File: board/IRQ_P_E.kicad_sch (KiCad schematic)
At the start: 19 parts, among them U14 74F32, U15 74F00, U23 74F11, U37 74LS148, U38 74LS08, U39 74LS148, U40 74F157, U51 74F157, U60 CY7C192, U61 CY7C192

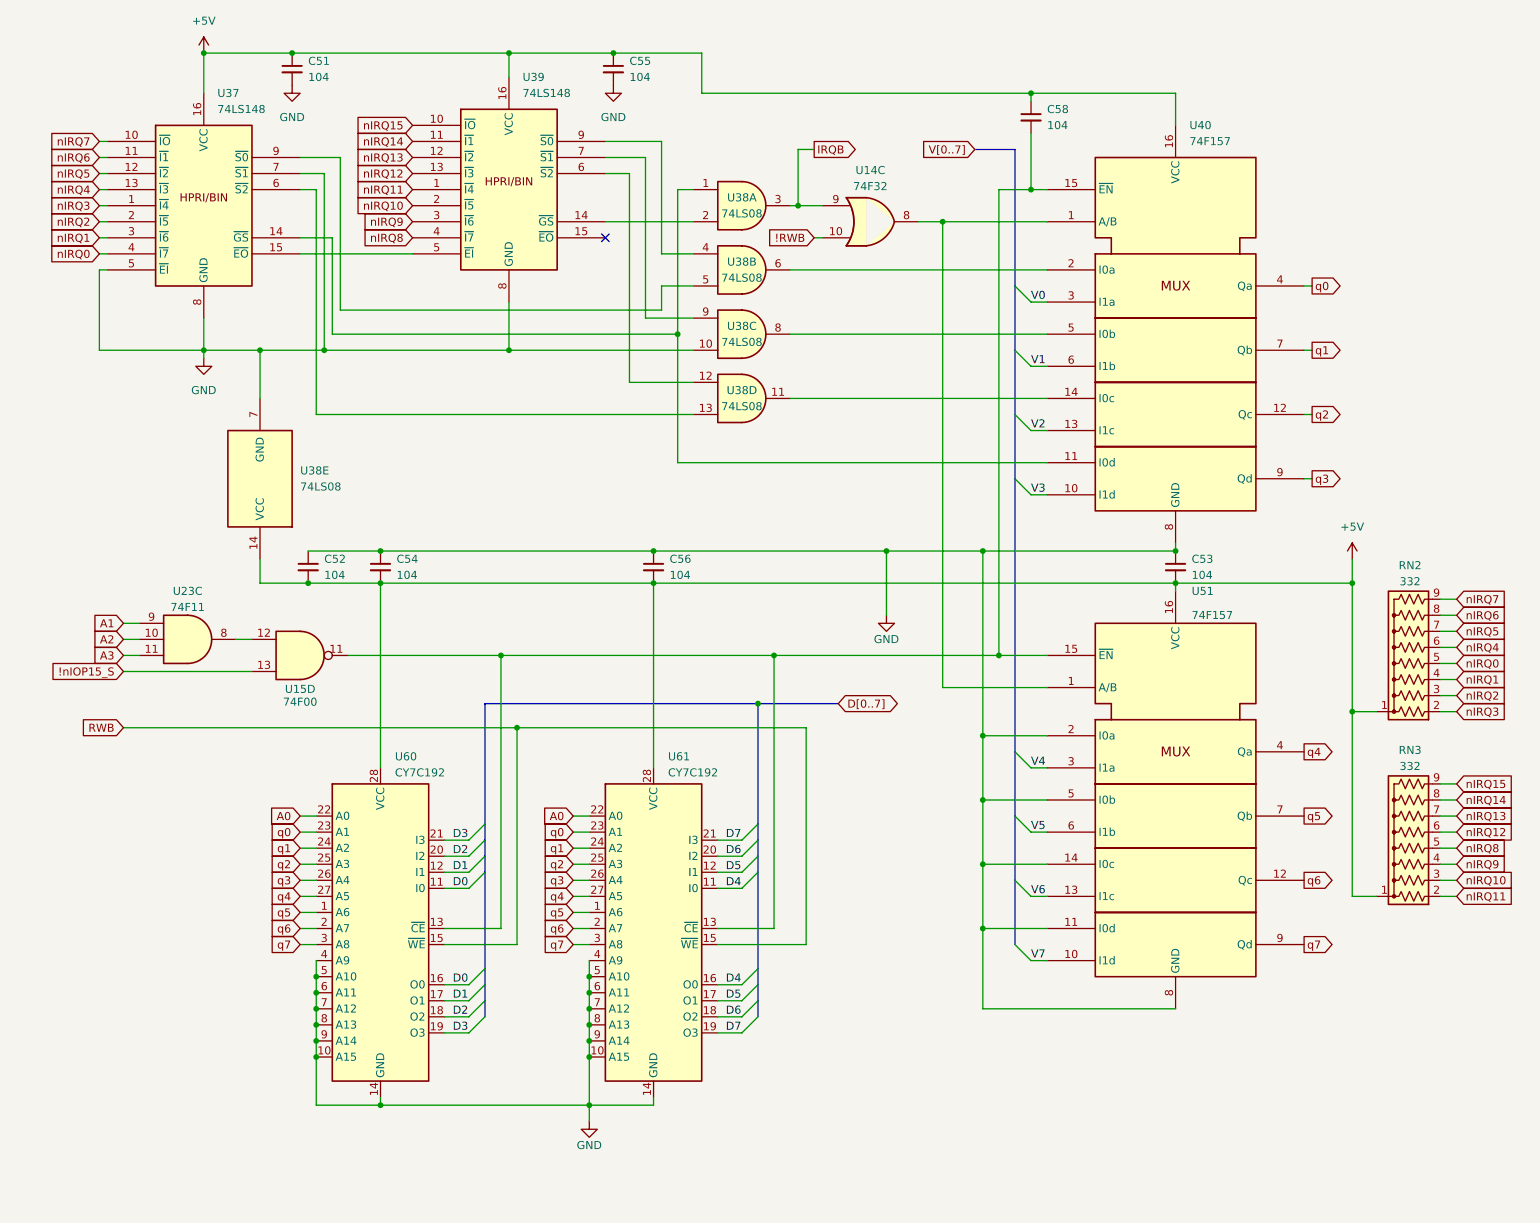
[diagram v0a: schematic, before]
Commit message: V2.0: wait states, GAL glue logic, serial clock and review fixes
Main board schematic:
- Replace the T4-T7 clock divider with RDY wait states. Fixed 7.16 MHz
  CPU clock; J36 selects 3.58 MHz for Rockwell parts. Waits are set per
  region through the write-only register at $FFF5 (reset = 3 waits).
- Move address decode, strobes, the wait-state generator, the IRQ
  encoder/latch/vector mux, ROM bank gating and DMA sync into seven GALs
  (U81-U86 ATF22V10C, U87 ATF16V8C), removing 29 ICs. CUPL sources,
  JEDECs and notes are in board/PLDs/V2.
- 1.8432 MHz serial clock, soft-power latch, -5V regulator, bulk caps,
  pull-ups, audio coupling/decoupling, GNDA tie, read-only Z register
  and other design-review fixes.
- New WaitStates and Support sheets; project symbol library
  hydra16.kicad_sym with sym-lib-table.

PCB updated from the schematic. Includes pending changes to the counter,
bus breakout and memory daughter card projects.

Firmware:
- Remove S_REGISTER; T/U/V/W now at $FFF0-$FFF3 to match the hardware.
- Add math.s and sound.s (included by os_main.s).
- Rebuild the 65C02 ROM image.

Co-Authored-By: Claude Opus 5.5 <noreply@anthropic.com>
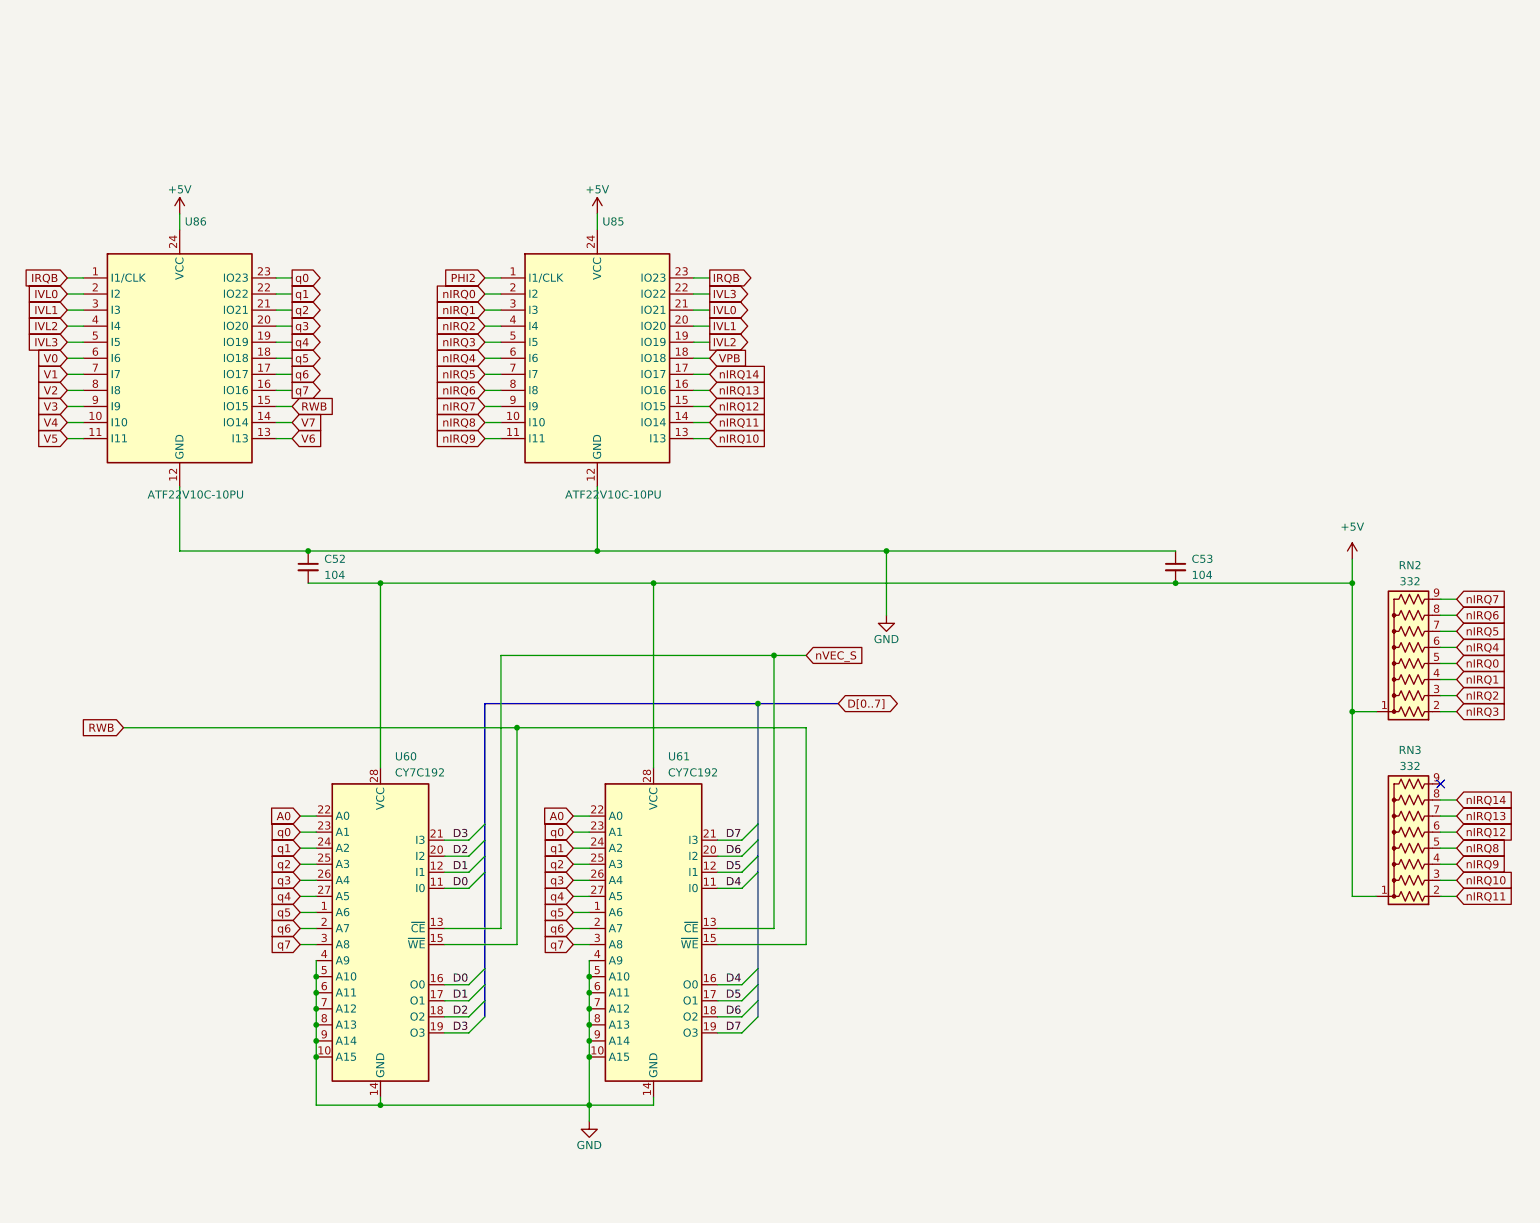
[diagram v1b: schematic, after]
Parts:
- removed C51, C54, C55, C56, C58: 104, Capacitor_THT:C_Disc_D5.0mm_W2.5mm_P5.00mm, symbol Device:C_Small
- removed U14: 74F32, Package_DIP:DIP-14_W7.62mm_Socket_LongPads, symbol 74xx:74LS32
- removed U15: 74F00, Package_DIP:DIP-14_W7.62mm_Socket_LongPads, symbol 74xx:74LS00
- removed U23: 74F11, Package_DIP:DIP-14_W7.62mm_Socket_LongPads, symbol 74xx:74LS11
- removed U37, U39: 74LS148, Package_DIP:DIP-16_W7.62mm_Socket_LongPads, symbol 74xx_IEEE:74148
- removed U38: 74LS08, Package_DIP:DIP-14_W7.62mm_Socket_LongPads, symbol 74xx:74LS08
- removed U40, U51: 74F157, Package_DIP:DIP-16_W7.62mm_Socket_LongPads, symbol 74xx_IEEE:74157
- added U85, U86: ATF22V10C-10PU, Package_DIP:DIP-24_W7.62mm_Socket_LongPads, symbol Hydra16:ATF22V10C
- U60, U61: footprint Package_DIP:DIP-28_W15.24mm_Socket_LongPads -> Package_DIP:DIP-28_W7.62mm_Socket_LongPads; symbol 65XX:6551 -> Hydra16:CY7C192
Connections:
- net +5V: now also U85.24 (VCC), U86.24 (VCC)
- net GND: now also U85.12 (GND), U86.12 (GND)
- net IRQB: now also U85.23 (IO23), U86.1 (I1/CLK)
- net RWB: now also U86.15 (IO15)
- net V0: now also U86.6 (I6)
- net V1: now also U86.7 (I7)
- net V2: now also U86.8 (I8)
- net V3: now also U86.9 (I9)
- net V4: now also U86.10 (I10)
- net V5: now also U86.11 (I11)
- net V6: now also U86.13 (I13)
- net V7: now also U86.14 (IO14)
- net nIRQ0: now also U85.2 (I2)
- net nIRQ1: now also U85.3 (I3)
- net nIRQ10: now also U85.13 (I13)
- net nIRQ11: now also U85.14 (IO14)
- net nIRQ12: now also U85.15 (IO15)
- net nIRQ13: now also U85.16 (IO16)
- net nIRQ14: now also U85.17 (IO17)
- net nIRQ2: now also U85.4 (I4)
- net nIRQ3: now also U85.5 (I5)
- net nIRQ4: now also U85.6 (I6)
- net nIRQ5: now also U85.7 (I7)
- net nIRQ6: now also U85.8 (I8)
- net nIRQ7: now also U85.9 (I9)
- net nIRQ8: now also U85.10 (I10)
- net nIRQ9: now also U85.11 (I11)
- net q0: now also U86.23 (IO23)
- net q1: now also U86.22 (IO22)
- net q2: now also U86.21 (IO21)
- net q3: now also U86.20 (IO20)
- net q4: now also U86.19 (IO19)
- net q5: now also U86.18 (IO18)
- net q6: now also U86.17 (IO17)
- net q7: now also U86.16 (IO16)
- net nVEC_S: now reaches U60.13 (~{CE}), U61.13 (~{CE})
- net nIRQ15: no longer names the net of RN3.9 (R8)
- new net IVL0: U85.21 (IO21), U86.2 (I2)
- new net IVL1: U85.20 (IO20), U86.3 (I3)
- new net IVL2: U85.19 (IO19), U86.4 (I4)
- new net IVL3: U85.22 (IO22), U86.5 (I5)
- new net PHI2: U85.1 (I1/CLK)
- new net VPB: U85.18 (IO18)

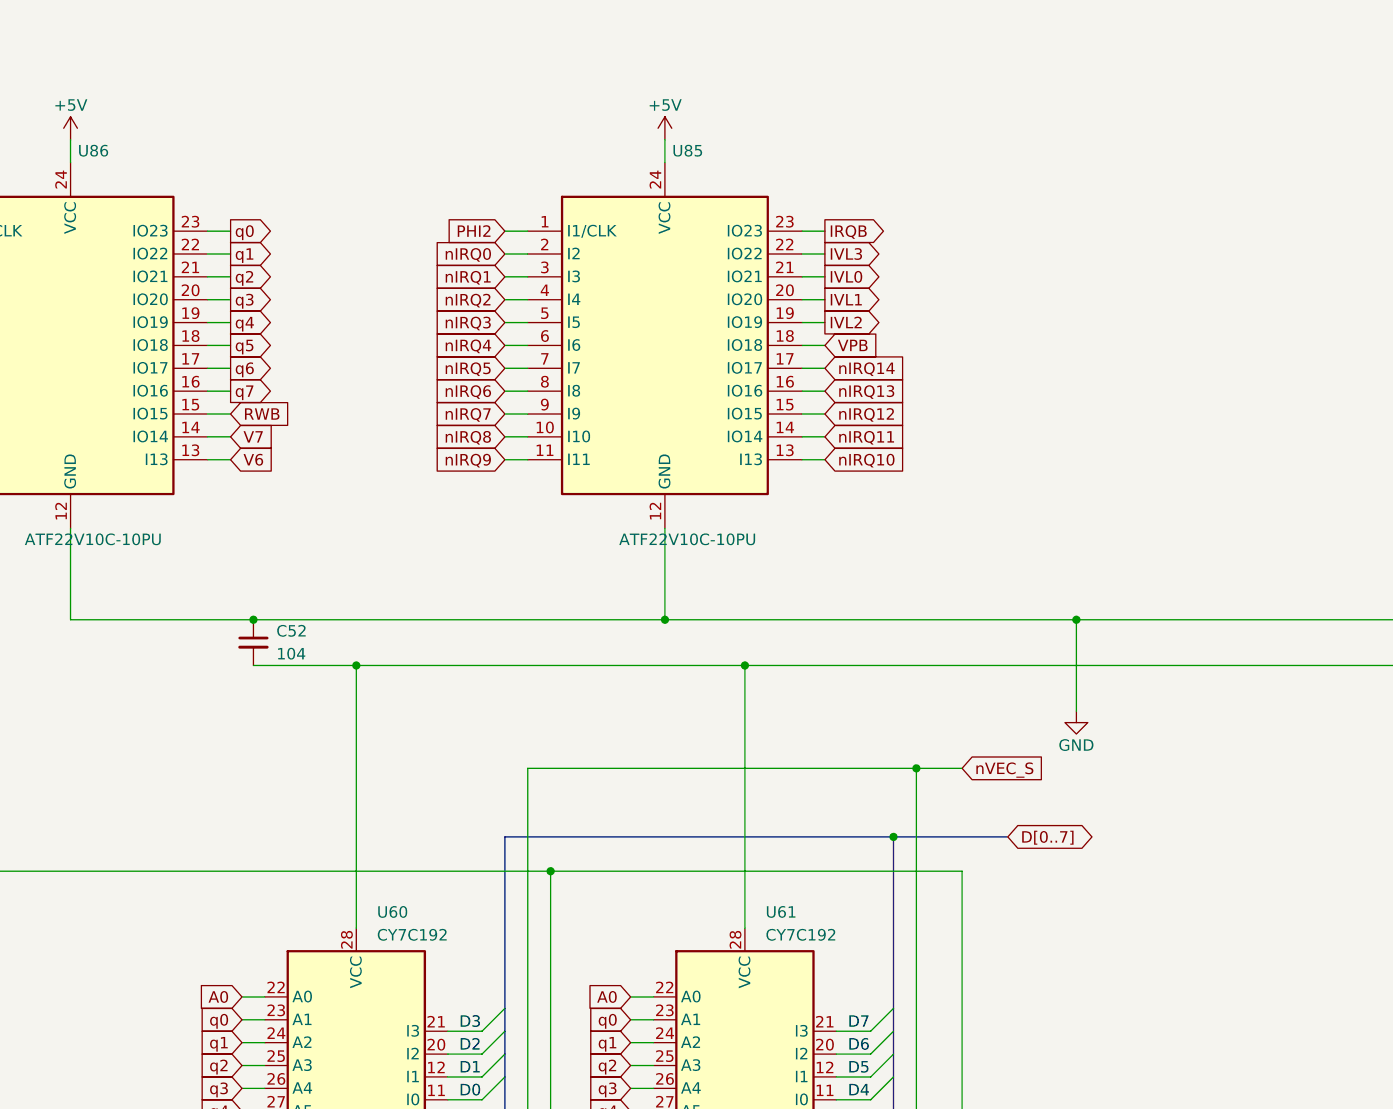
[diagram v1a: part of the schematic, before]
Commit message: V2.0 rev 2.0D: clock stretching, OS ROM paging and review fixes
Bus timing:
- New GAL C (U88) generates PHI2/PHI1 and the 3.58 MHz sound clock from
  the 14.318 MHz master, replacing the U35 74F191 divider. J36 now selects
  7.16 or 3.58 MHz.
- Banked RAM, banked ROM and slot I/O ($FF20-$FFEF) get one extra PHI2-low
  period plus 0-3 extra PHI2-high periods set in $FFF5 (GAL D). This
  replaces the on-board RDY wait generator; cards can still pull RDY.
- Write strobes are now hold-time safe: PHI1 comes straight from GAL C
  and RWB_M straight from GAL B2.

Review fixes:
- OS ROM chip enable from a single-level decode, output enable from
  GAL B1; -55 part specified. Full 4K OS ROM paging via GAL G.
- Vector RAM writes only during PHI2; $FFF0-$FFFF no longer slowed.
- YM2151 /WR on RWB_M. U62 removed. RB0-RB7 pull-ups (RN5).
- Slot clocks driven through U56 and U34 with 33R series resistors.
- J38 enables in-system flashing of the banked ROMs.
- W65C22S/W65C51N, AS6C4008, DS1813-5 and CY7C192-25 values; R4 1k.
- J7 pin 8 no longer +5V; +5VA renamed +5VSB; serial handshake loop.
- Sheet titles and revisions, slot symbol pin fixes, and project symbol
  and footprint libraries so the project opens on another machine.

Co-Authored-By: Claude Opus 5.5 <noreply@anthropic.com>
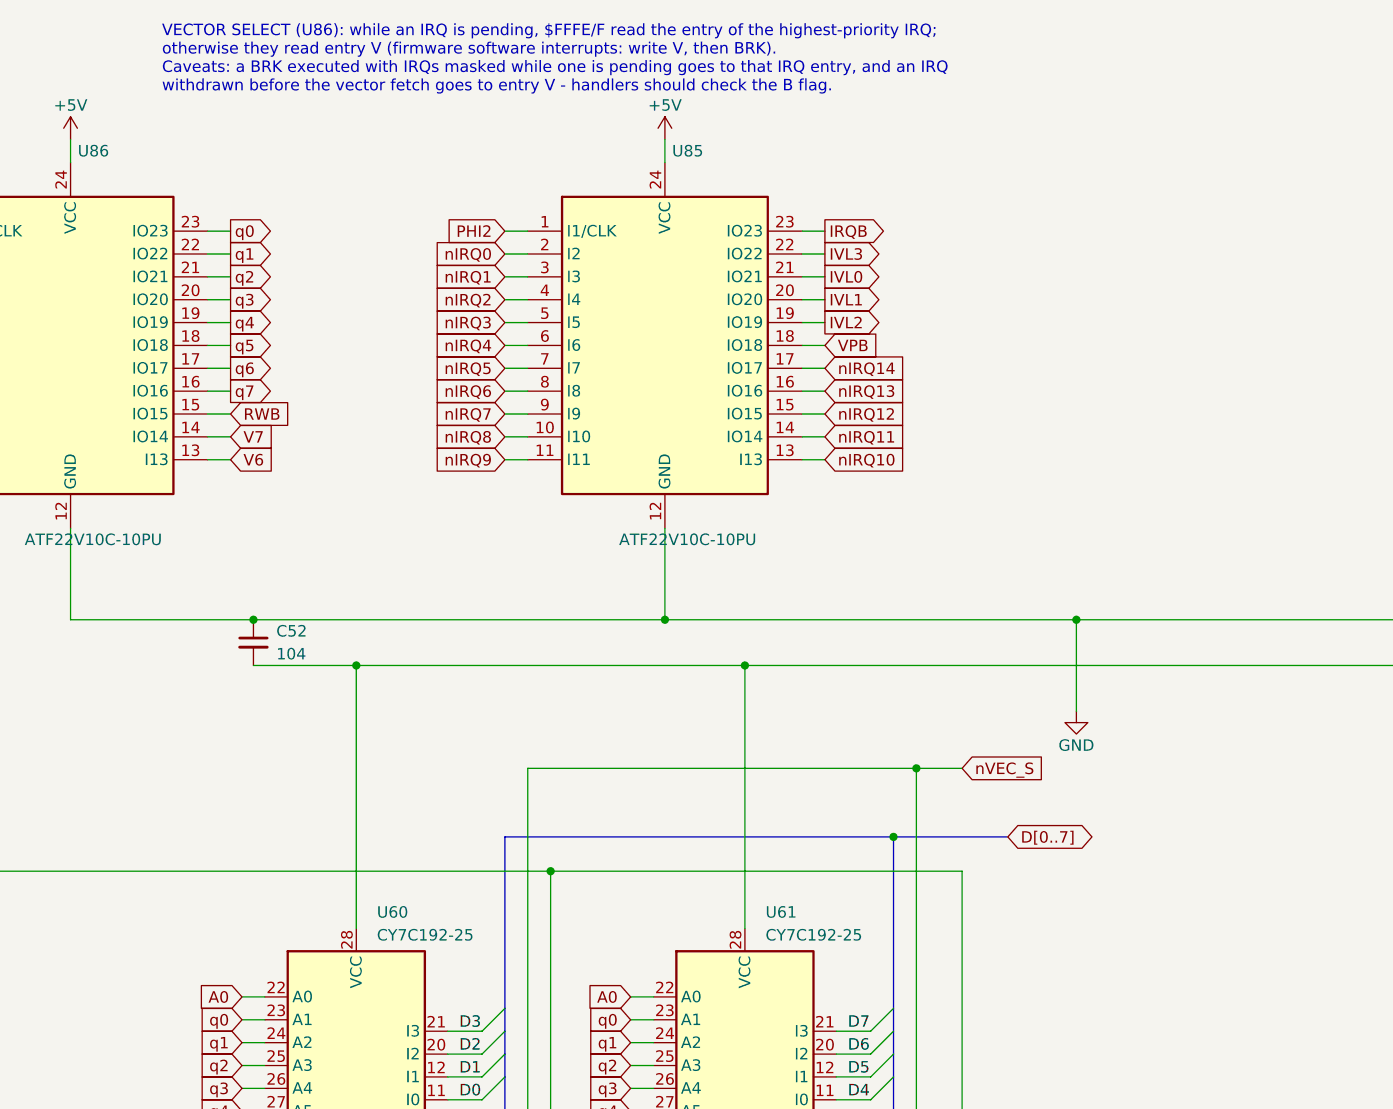
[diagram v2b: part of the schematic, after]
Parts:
- U60, U61: value CY7C192 -> CY7C192-25
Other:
- note added: "VECTOR SELECT (U86): while an IRQ is pending, $FFFE/F read the entry of the highest-priority IRQ; otherwise they read entry V (firmware software interrupts: write V, then BRK). Caveats: a BRK executed with IRQs masked while one is pending goes to that IRQ entry, and an IRQ withdrawn before the vector fetch goes to entry V - handlers should check the B flag."
- title: ZeroPage $00/$01 Mirror Memory and RAM/ROM Bank Logic -> Interrupt Priority Encoder and Vector RAM
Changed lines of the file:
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@@
 	(paper "USLetter")
 	(title_block
-		(title "ZeroPage $00/$01 Mirror Memory and RAM/ROM Bank Logic")
-		(date "2026-01-28")
-		(rev "2.0B")
+		(title "Interrupt Priority Encoder and Vector RAM")
+		(date "2026-10-06")
+		(rev "2.0D")
 		(company "Data Tuning")
 		(comment 1 "Hydra 16")
@@
 			)
 		)
-		(property "Value" "CY7C192"
+		(property "Value" "CY7C192-25"
 			(at 84.836 134.112 0)
 			(effects
@@
 			)
 		)
-		(property "Value" "CY7C192"
+		(property "Value" "CY7C192-25"
 			(at 128.016 134.112 0)
 			(effects
@@
 		)
 	)
+	(text "VECTOR SELECT (U86): while an IRQ is pending, $FFFE/F read the entry of the highest-priority IRQ;\notherwise they read entry V (firmware software interrupts: write V, then BRK).\nCaveats: a BRK executed with IRQs masked while one is pending goes to that IRQ entry, and an IRQ\nwithdrawn before the vector fetch goes to entry V - handlers should check the B flag."
+		(exclude_from_sim no)
+		(at 60.96 33.02 0)
+		(effects
+			(font
+				(size 1.27 1.27)
+			)
+			(justify left top)
+		)
+	)
